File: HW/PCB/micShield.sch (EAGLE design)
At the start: 32 parts, among them M1 PMM-3738-VM1010-R, U1 LM27762DSSR, U2 LT6002CGN

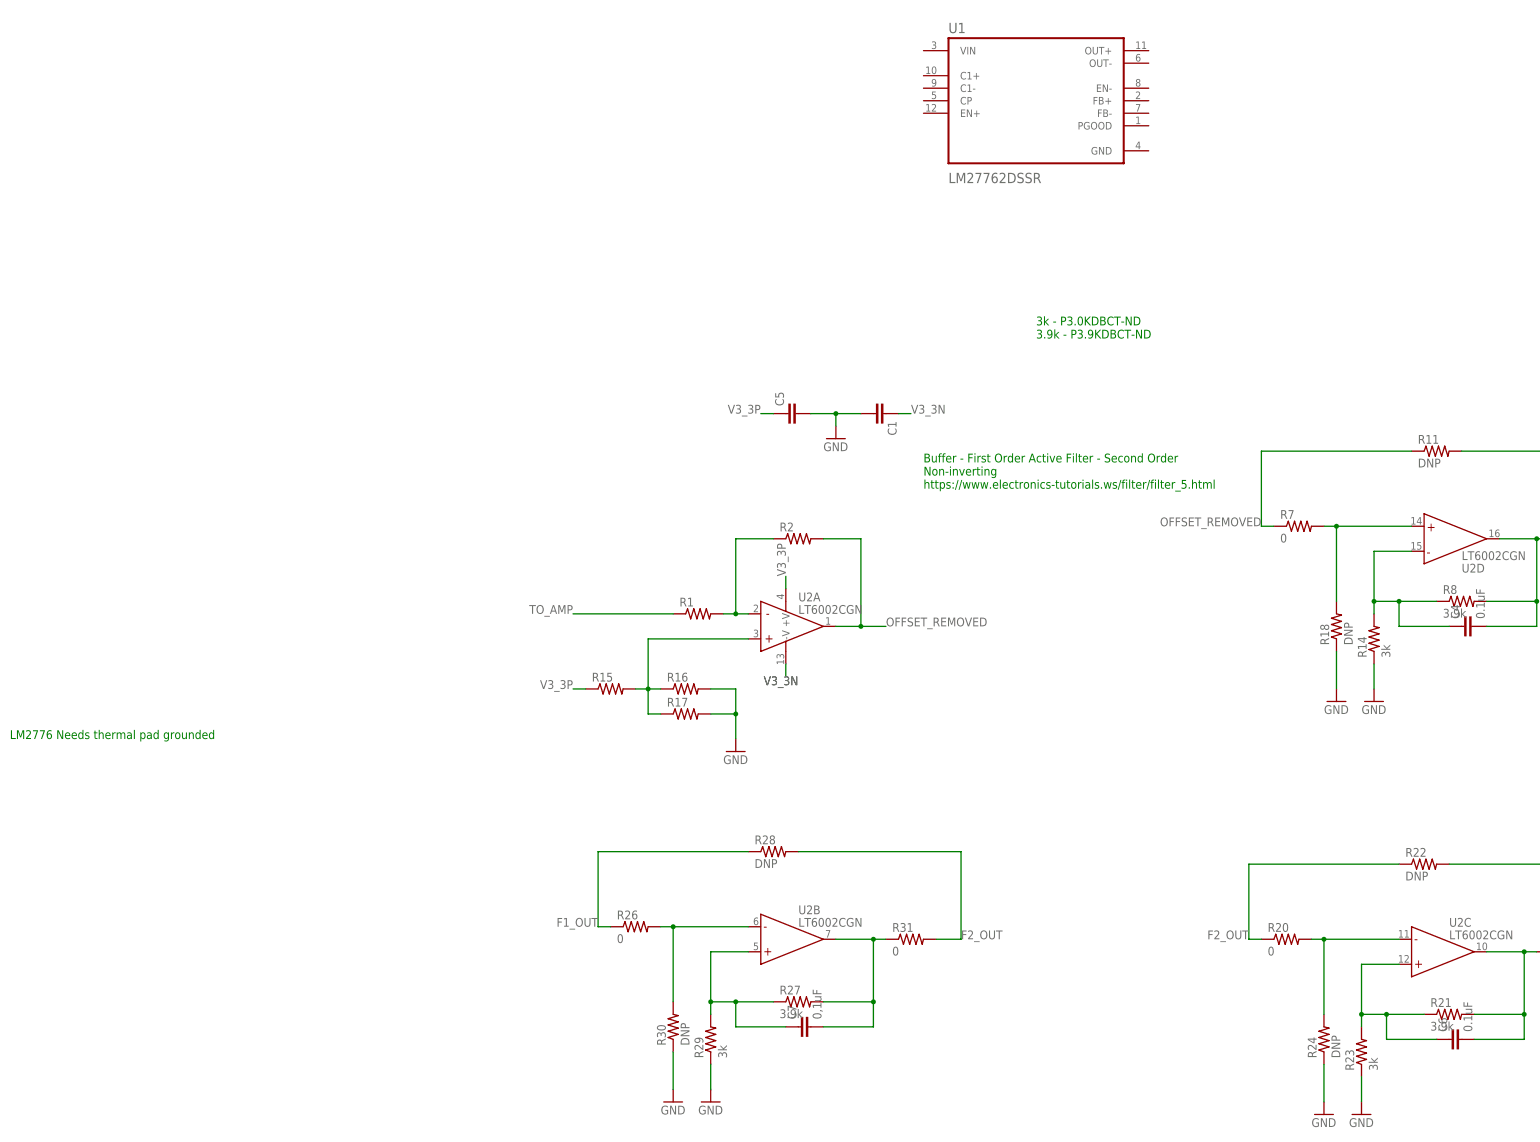
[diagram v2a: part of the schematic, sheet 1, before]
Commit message: More updates to the PCB. Added +/-3V
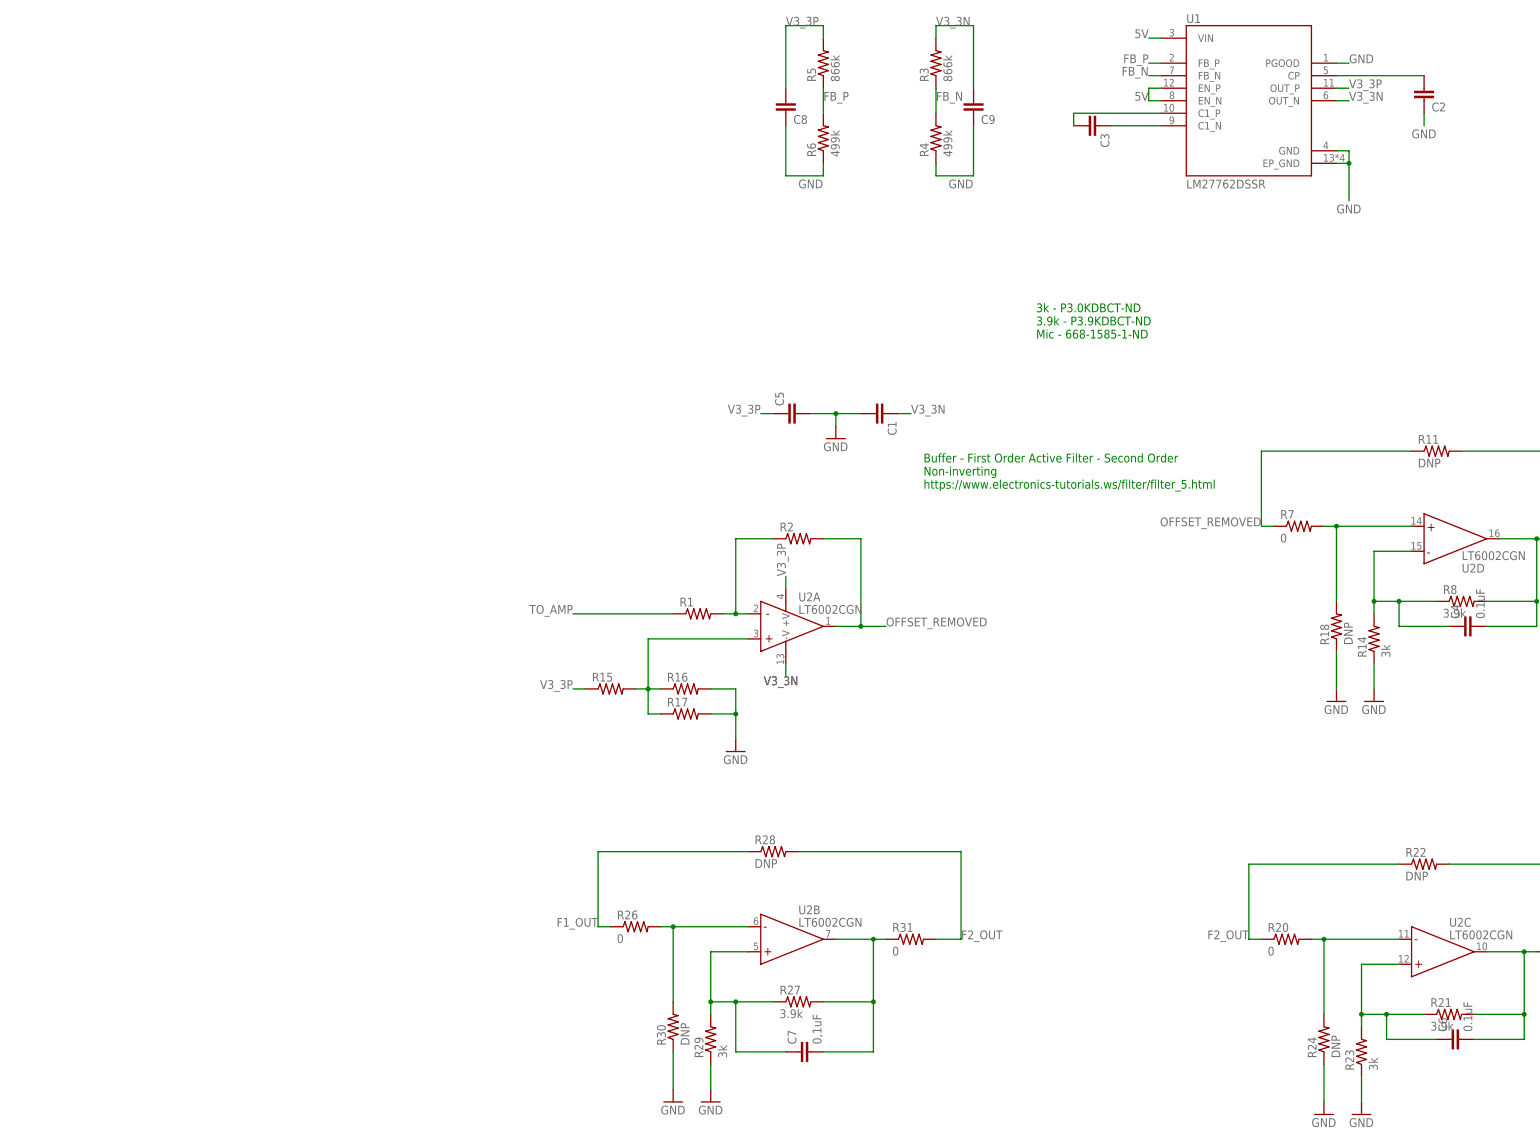
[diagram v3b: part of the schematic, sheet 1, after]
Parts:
- added C2, C8, C9: (no value), SparkFun-Capacitors:CAP0603-CAP
- added C3: (no value), SparkFun-Capacitors:CAP0402-CAP
- added R3, R5: 866k, SparkFun-Resistors:RESISTOR0402
- added R4, R6: 499k, SparkFun-Resistors:RESISTOR0402
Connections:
- new net 5V: U1.EN_N, U1.EN_P, U1.VIN
- new net FB_N: R3.1, R4.2, U1.FB_N
- new net FB_P: R5.1, R6.2, U1.FB_P
- new net N$2: C2.2, U1.CP
- new net N$3: C3.1, U1.C1_N
- new net N$4: C3.2, U1.C1_P
- net GND: now also C2.1, C8.1, C9.1, R4.1, R6.1, U1.EP_GND, U1.GND, U1.PGOOD
- net V3_3N: now also C9.2, R3.2, U1.OUT_N
- net V3_3P: now also C8.2, R5.2, U1.OUT_P
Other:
- note added: "3k - P3.0KDBCT-ND 3.9k - P3.9KDBCT-ND Mic - 668-1585-1-ND"
- note removed: "3k - P3.0KDBCT-ND 3.9k - P3.9KDBCT-ND"
- note removed: "LM2776 Needs thermal pad grounded"
- moved on the sheet: C7
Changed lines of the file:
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@@
 <part name="GND3" library="SparkFun-Aesthetics" deviceset="GND" device=""/>
 <part name="U1" library="LM27762DSSR" deviceset="LM27762DSSR" device=""/>
+<part name="C2" library="SparkFun-Capacitors" deviceset="CAP" device="0603-CAP"/>
+<part name="C3" library="SparkFun-Capacitors" deviceset="CAP" device="0402-CAP"/>
+<part name="R3" library="SparkFun-Resistors" deviceset="RESISTOR" device="0402" value="866k"/>
+<part name="R4" library="SparkFun-Resistors" deviceset="RESISTOR" device="0402" value="499k"/>
+<part name="R5" library="SparkFun-Resistors" deviceset="RESISTOR" device="0402" value="866k"/>
+<part name="R6" library="SparkFun-Resistors" deviceset="RESISTOR" device="0402" value="499k"/>
+<part name="C8" library="SparkFun-Capacitors" deviceset="CAP" device="0603-CAP"/>
+<part name="C9" library="SparkFun-Capacitors" deviceset="CAP" device="0603-CAP"/>
 </parts>
 <sheets>
@@
 https://www.electronics-tutorials.ws/filter/filter_5.html</text>
 <text x="78.74" y="119.38" size="1.778" layer="91">3k - P3.0KDBCT-ND
-3.9k - P3.9KDBCT-ND</text>
-<text x="-129.54" y="38.1" size="1.778" layer="91">LM2776 Needs thermal pad grounded</text>
+3.9k - P3.9KDBCT-ND
+Mic - 668-1585-1-ND</text>
 </plain>
 <instances>
@@
 <instance part="R26" gate="G$1" x="-2.54" y="0"/>
 <instance part="R27" gate="G$1" x="30.48" y="-15.24"/>
-<instance part="C7" gate="G$1" x="33.02" y="-20.32" rot="R90"/>
+<instance part="C7" gate="G$1" x="33.02" y="-25.4" rot="R90"/>
 <instance part="GND8" gate="1" x="12.7" y="-35.56"/>
 <instance part="R28" gate="G$1" x="25.4" y="15.24"/>
@@
 <instance part="C1" gate="G$1" x="45.72" y="104.14" rot="R270"/>
 <instance part="GND3" gate="1" x="38.1" y="99.06"/>
-<instance part="U1" gate="G$1" x="78.74" y="167.64"/>
+<instance part="U1" gate="G$1" x="121.92" y="167.64"/>
+<instance part="C2" gate="G$1" x="157.48" y="170.18" smashed="yes" rot="R180">
+<attribute name="NAME" x="159.004" y="167.259" size="1.778" layer="95" rot="MR180"/>
+<attribute name="VALUE" x="159.004" y="172.339" size="1.778" layer="96" rot="MR180"/>
+</instance>
+<instance part="C3" gate="G$1" x="88.9" y="162.56" rot="R270"/>
+<instance part="R3" gate="G$1" x="58.42" y="175.26" rot="R90"/>
+<instance part="R4" gate="G$1" x="58.42" y="160.02" rot="R90"/>
+<instance part="R5" gate="G$1" x="35.56" y="175.26" rot="R90"/>
+<instance part="R6" gate="G$1" x="35.56" y="160.02" rot="R90"/>
+<instance part="C8" gate="G$1" x="27.94" y="167.64" smashed="yes" rot="R180">
+<attribute name="NAME" x="29.464" y="164.719" size="1.778" layer="95" rot="MR180"/>
+<attribute name="VALUE" x="29.464" y="169.799" size="1.778" layer="96" rot="MR180"/>
+</instance>
+<instance part="C9" gate="G$1" x="66.04" y="167.64" smashed="yes" rot="R180">
+<attribute name="NAME" x="67.564" y="164.719" size="1.778" layer="95" rot="MR180"/>
+<attribute name="VALUE" x="67.564" y="169.799" size="1.778" layer="96" rot="MR180"/>
+</instance>
 </instances>
 <busses>
@@
 <wire x1="38.1" y1="104.14" x2="43.18" y2="104.14" width="0.1524" layer="91"/>
 </segment>
+<segment>
+<pinref part="U1" gate="G$1" pin="GND"/>
+<wire x1="139.7" y1="157.48" x2="142.24" y2="157.48" width="0.1524" layer="91"/>
+<wire x1="142.24" y1="157.48" x2="142.24" y2="154.94" width="0.1524" layer="91"/>
+<pinref part="U1" gate="G$1" pin="EP_GND"/>
+<wire x1="142.24" y1="154.94" x2="142.24" y2="147.32" width="0.1524" layer="91"/>
+<wire x1="139.7" y1="154.94" x2="142.24" y2="154.94" width="0.1524" layer="91"/>
+<junction x="142.24" y="154.94"/>
+<label x="139.7" y="144.78" size="1.778" layer="95"/>
+</segment>
+<segment>
+<pinref part="U1" gate="G$1" pin="PGOOD"/>
+<wire x1="139.7" y1="175.26" x2="142.24" y2="175.26" width="0.1524" layer="91"/>
+<label x="142.24" y="175.26" size="1.778" layer="95"/>
+</segment>
+<segment>
+<pinref part="C2" gate="G$1" pin="1"/>
+<wire x1="157.48" y1="165.1" x2="157.48" y2="162.56" width="0.1524" layer="91"/>
+<label x="154.94" y="160.02" size="1.778" layer="95"/>
+</segment>
+<segment>
+<pinref part="R6" gate="G$1" pin="1"/>
+<wire x1="35.56" y1="154.94" x2="35.56" y2="152.4" width="0.1524" layer="91"/>
+<label x="30.48" y="149.86" size="1.778" layer="95"/>
+<pinref part="C8" gate="G$1" pin="1"/>
+<wire x1="27.94" y1="162.56" x2="27.94" y2="152.4" width="0.1524" layer="91"/>
+<wire x1="27.94" y1="152.4" x2="35.56" y2="152.4" width="0.1524" layer="91"/>
+</segment>
+<segment>
+<pinref part="R4" gate="G$1" pin="1"/>
+<wire x1="58.42" y1="154.94" x2="58.42" y2="152.4" width="0.1524" layer="91"/>
+<label x="60.96" y="149.86" size="1.778" layer="95"/>
+<wire x1="58.42" y1="152.4" x2="66.04" y2="152.4" width="0.1524" layer="91"/>
+<pinref part="C9" gate="G$1" pin="1"/>
+<wire x1="66.04" y1="152.4" x2="66.04" y2="162.56" width="0.1524" layer="91"/>
+</segment>
 </net>
 <net name="TO_AMP" class="0">
@@
 <wire x1="25.4" y1="104.14" x2="22.86" y2="104.14" width="0.1524" layer="91"/>
 <label x="22.86" y="104.14" size="1.778" layer="95" rot="MR0"/>
+</segment>
+<segment>
+<pinref part="U1" gate="G$1" pin="OUT_P"/>
+<wire x1="139.7" y1="170.18" x2="142.24" y2="170.18" width="0.1524" layer="91"/>
+<label x="142.24" y="170.18" size="1.778" layer="95"/>
+</segment>
+<segment>
+<pinref part="R5" gate="G$1" pin="2"/>
+<wire x1="35.56" y1="180.34" x2="35.56" y2="182.88" width="0.1524" layer="91"/>
+<label x="27.94" y="182.88" size="1.778" layer="95"/>
+<wire x1="35.56" y1="182.88" x2="27.94" y2="182.88" width="0.1524" layer="91"/>
+<pinref part="C8" gate="G$1" pin="2"/>
+<wire x1="27.94" y1="182.88" x2="27.94" y2="170.18" width="0.1524" layer="91"/>
 </segment>
 </net>
@@
 <wire x1="50.8" y1="104.14" x2="53.34" y2="104.14" width="0.1524" layer="91"/>
 <label x="53.34" y="104.14" size="1.778" layer="95"/>
+</segment>
+<segment>
+<pinref part="U1" gate="G$1" pin="OUT_N"/>
+<wire x1="139.7" y1="167.64" x2="142.24" y2="167.64" width="0.1524" layer="91"/>
+<label x="142.24" y="167.64" size="1.778" layer="95"/>
+</segment>
+<segment>
+<pinref part="R3" gate="G$1" pin="2"/>
+<wire x1="58.42" y1="180.34" x2="58.42" y2="182.88" width="0.1524" layer="91"/>
+<label x="58.42" y="182.88" size="1.778" layer="95"/>
+<wire x1="58.42" y1="182.88" x2="66.04" y2="182.88" width="0.1524" layer="91"/>
+<pinref part="C9" gate="G$1" pin="2"/>
+<wire x1="66.04" y1="182.88" x2="66.04" y2="170.18" width="0.1524" layer="91"/>
 </segment>
 </net>
@@
 <pinref part="C7" gate="G$1" pin="1"/>
 <wire x1="17.78" y1="-15.24" x2="25.4" y2="-15.24" width="0.1524" layer="91"/>
-<wire x1="27.94" y1="-20.32" x2="17.78" y2="-20.32" width="0.1524" layer="91"/>
-<wire x1="17.78" y1="-20.32" x2="17.78" y2="-15.24" width="0.1524" layer="91"/>
+<wire x1="27.94" y1="-25.4" x2="17.78" y2="-25.4" width="0.1524" layer="91"/>
+<wire x1="17.78" y1="-25.4" x2="17.78" y2="-15.24" width="0.1524" layer="91"/>
 <junction x="12.7" y="-15.24"/>
 <junction x="17.78" y="-15.24"/>
@@
 <pinref part="R27" gate="G$1" pin="2"/>
 <wire x1="35.56" y1="-15.24" x2="45.72" y2="-15.24" width="0.1524" layer="91"/>
-<wire x1="45.72" y1="-15.24" x2="45.72" y2="-20.32" width="0.1524" layer="91"/>
+<wire x1="45.72" y1="-15.24" x2="45.72" y2="-25.4" width="0.1524" layer="91"/>
 <pinref part="C7" gate="G$1" pin="2"/>
-<wire x1="45.72" y1="-20.32" x2="35.56" y2="-20.32" width="0.1524" layer="91"/>
+<wire x1="45.72" y1="-25.4" x2="35.56" y2="-25.4" width="0.1524" layer="91"/>
 <junction x="45.72" y="-15.24"/>
 <wire x1="45.72" y1="-15.24" x2="45.72" y2="-2.54" width="0.1524" layer="91"/>
@@
 </segment>
 </net>
+<net name="5V" class="0">
+<segment>
+<pinref part="U1" gate="G$1" pin="VIN"/>
+<wire x1="104.14" y1="180.34" x2="101.6" y2="180.34" width="0.1524" layer="91"/>
+<label x="101.6" y="180.34" size="1.778" layer="95" rot="MR0"/>
+</segment>
+<segment>
+<pinref part="U1" gate="G$1" pin="EN_P"/>
+<wire x1="104.14" y1="170.18" x2="101.6" y2="170.18" width="0.1524" layer="91"/>
+<wire x1="101.6" y1="170.18" x2="101.6" y2="167.64" width="0.1524" layer="91"/>
+<pinref part="U1" gate="G$1" pin="EN_N"/>
+<wire x1="101.6" y1="167.64" x2="104.14" y2="167.64" width="0.1524" layer="91"/>
+<label x="101.6" y="167.64" size="1.778" layer="95" rot="MR0"/>
+</segment>
+</net>
+<net name="N$2" class="0">
+<segment>
+<pinref part="U1" gate="G$1" pin="CP"/>
+<pinref part="C2" gate="G$1" pin="2"/>
+<wire x1="139.7" y1="172.72" x2="157.48" y2="172.72" width="0.1524" layer="91"/>
+</segment>
+</net>
+<net name="N$3" class="0">
+<segment>
+<pinref part="C3" gate="G$1" pin="1"/>
+<pinref part="U1" gate="G$1" pin="C1_N"/>
+<wire x1="93.98" y1="162.56" x2="104.14" y2="162.56" width="0.1524" layer="91"/>
+</segment>
+</net>
+<net name="N$4" class="0">
+<segment>
+<pinref part="U1" gate="G$1" pin="C1_P"/>
+<wire x1="104.14" y1="165.1" x2="86.36" y2="165.1" width="0.1524" layer="91"/>
+<pinref part="C3" gate="G$1" pin="2"/>
+<wire x1="86.36" y1="165.1" x2="86.36" y2="162.56" width="0.1524" layer="91"/>
+</segment>
+</net>
+<net name="FB_P" class="0">
+<segment>
+<pinref part="U1" gate="G$1" pin="FB_P"/>
+<wire x1="104.14" y1="175.26" x2="101.6" y2="175.26" width="0.1524" layer="91"/>
+<label x="101.6" y="175.26" size="1.778" layer="95" rot="MR0"/>
+</segment>
+<segment>
+<pinref part="R5" gate="G$1" pin="1"/>
+<pinref part="R6" gate="G$1" pin="2"/>
+<wire x1="35.56" y1="170.18" x2="35.56" y2="165.1" width="0.1524" layer="91"/>
+<label x="35.56" y="167.64" size="1.778" layer="95"/>
+</segment>
+</net>
+<net name="FB_N" class="0">
+<segment>
+<pinref part="U1" gate="G$1" pin="FB_N"/>
+<wire x1="104.14" y1="172.72" x2="101.6" y2="172.72" width="0.1524" layer="91"/>
+<label x="101.6" y="172.72" size="1.778" layer="95" rot="MR0"/>
+</segment>
+<segment>
+<pinref part="R3" gate="G$1" pin="1"/>
+<pinref part="R4" gate="G$1" pin="2"/>
+<wire x1="58.42" y1="170.18" x2="58.42" y2="165.1" width="0.1524" layer="91"/>
+<label x="58.42" y="167.64" size="1.778" layer="95"/>
+</segment>
+</net>

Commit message: Schematics and Layout updates.
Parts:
- added C10: (no value), SparkFun-Capacitors:CAP0603-CAP
- added R10, R9: (no value), SparkFun-Resistors:RESISTOR0402
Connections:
- new net N$11: R10.2, U$1.VIN
- new net N$5: R9.2, U$1.VUSB
- net 5V: now also C10.2, R10.1, R9.1
- net FILTERED_OUT: now also U$1.14/A0
- net GND: now also C10.1, U$1.AGND, U$1.GND, U$1.GND2
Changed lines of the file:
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@@
 <part name="C8" library="SparkFun-Capacitors" deviceset="CAP" device="0603-CAP"/>
 <part name="C9" library="SparkFun-Capacitors" deviceset="CAP" device="0603-CAP"/>
+<part name="C10" library="SparkFun-Capacitors" deviceset="CAP" device="0603-CAP"/>
+<part name="R9" library="SparkFun-Resistors" deviceset="RESISTOR" device="0402"/>
+<part name="R10" library="SparkFun-Resistors" deviceset="RESISTOR" device="0402"/>
 </parts>
 <sheets>
@@
 <attribute name="VALUE" x="67.564" y="169.799" size="1.778" layer="96" rot="MR180"/>
 </instance>
+<instance part="C10" gate="G$1" x="83.82" y="177.8" smashed="yes" rot="R180">
+<attribute name="NAME" x="85.344" y="174.879" size="1.778" layer="95" rot="MR180"/>
+<attribute name="VALUE" x="85.344" y="179.959" size="1.778" layer="96" rot="MR180"/>
+</instance>
+<instance part="R9" gate="G$1" x="335.28" y="78.74" rot="R90"/>
+<instance part="R10" gate="G$1" x="327.66" y="73.66" rot="R180"/>
 </instances>
 <busses>
@@
 <wire x1="66.04" y1="152.4" x2="66.04" y2="162.56" width="0.1524" layer="91"/>
 </segment>
+<segment>
+<pinref part="C10" gate="G$1" pin="1"/>
+<wire x1="83.82" y1="172.72" x2="83.82" y2="170.18" width="0.1524" layer="91"/>
+<label x="81.28" y="167.64" size="1.778" layer="95"/>
+</segment>
+<segment>
+<pinref part="U$1" gate="G$1" pin="GND"/>
+<wire x1="274.32" y1="73.66" x2="271.78" y2="73.66" width="0.1524" layer="91"/>
+<label x="271.78" y="73.66" size="1.778" layer="95" rot="MR0"/>
+</segment>
+<segment>
+<pinref part="U$1" gate="G$1" pin="AGND"/>
+<wire x1="314.96" y1="71.12" x2="317.5" y2="71.12" width="0.1524" layer="91"/>
+<label x="317.5" y="71.12" size="1.778" layer="95"/>
+</segment>
+<segment>
+<pinref part="U$1" gate="G$1" pin="GND2"/>
+<wire x1="314.96" y1="38.1" x2="317.5" y2="38.1" width="0.1524" layer="91"/>
+<label x="317.5" y="38.1" size="1.778" layer="95"/>
+</segment>
 </net>
 <net name="TO_AMP" class="0">
@@
 <pinref part="U2" gate="A" pin="+V"/>
 <wire x1="27.94" y1="68.58" x2="27.94" y2="71.12" width="0.1524" layer="91"/>
-<label x="27.94" y="71.12" size="1.778" layer="95" rot="R90"/>
+<label x="30.48" y="73.66" size="1.778" layer="95" rot="R180"/>
 </segment>
 <segment>
@@
 <label x="195.58" y="-5.08" size="1.778" layer="95"/>
 </segment>
+<segment>
+<pinref part="U$1" gate="G$1" pin="14/A0"/>
+<wire x1="314.96" y1="43.18" x2="317.5" y2="43.18" width="0.1524" layer="91"/>
+<label x="317.5" y="43.18" size="1.778" layer="95"/>
+</segment>
 </net>
 <net name="N$16" class="0">
@@
 <label x="101.6" y="167.64" size="1.778" layer="95" rot="MR0"/>
 </segment>
+<segment>
+<pinref part="C10" gate="G$1" pin="2"/>
+<wire x1="83.82" y1="180.34" x2="83.82" y2="182.88" width="0.1524" layer="91"/>
+<label x="83.82" y="182.88" size="1.778" layer="95"/>
+</segment>
+<segment>
+<pinref part="R9" gate="G$1" pin="1"/>
+<wire x1="340.36" y1="73.66" x2="335.28" y2="73.66" width="0.1524" layer="91"/>
+<pinref part="R10" gate="G$1" pin="1"/>
+<junction x="335.28" y="73.66"/>
+<wire x1="335.28" y1="73.66" x2="332.74" y2="73.66" width="0.1524" layer="91"/>
+<label x="340.36" y="73.66" size="1.778" layer="95"/>
+</segment>
 </net>
 <net name="N$2" class="0">
@@
 </segment>
 </net>
+<net name="N$5" class="0">
+<segment>
+<pinref part="U$1" gate="G$1" pin="VUSB"/>
+<pinref part="R9" gate="G$1" pin="2"/>
+<wire x1="335.28" y1="83.82" x2="335.28" y2="86.36" width="0.1524" layer="91"/>
+<wire x1="335.28" y1="86.36" x2="314.96" y2="86.36" width="0.1524" layer="91"/>
+</segment>
+</net>
+<net name="N$11" class="0">
+<segment>
+<pinref part="U$1" gate="G$1" pin="VIN"/>
+<pinref part="R10" gate="G$1" pin="2"/>
+<wire x1="314.96" y1="73.66" x2="322.58" y2="73.66" width="0.1524" layer="91"/>
+</segment>
+</net>
